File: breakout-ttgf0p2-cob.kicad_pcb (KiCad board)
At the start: 4 copper layers, 50 x 50 mm, 105 parts, among them J1 Conn_01x12, J2 DF12NB-60DS-0.5V_51, J3 DF12NB-50DS-0.5V_51, U1 AP2112K-3.3, U2 AP2112K-3.3, U3 TT_GF_0p2_ASIC, U4 24LC02

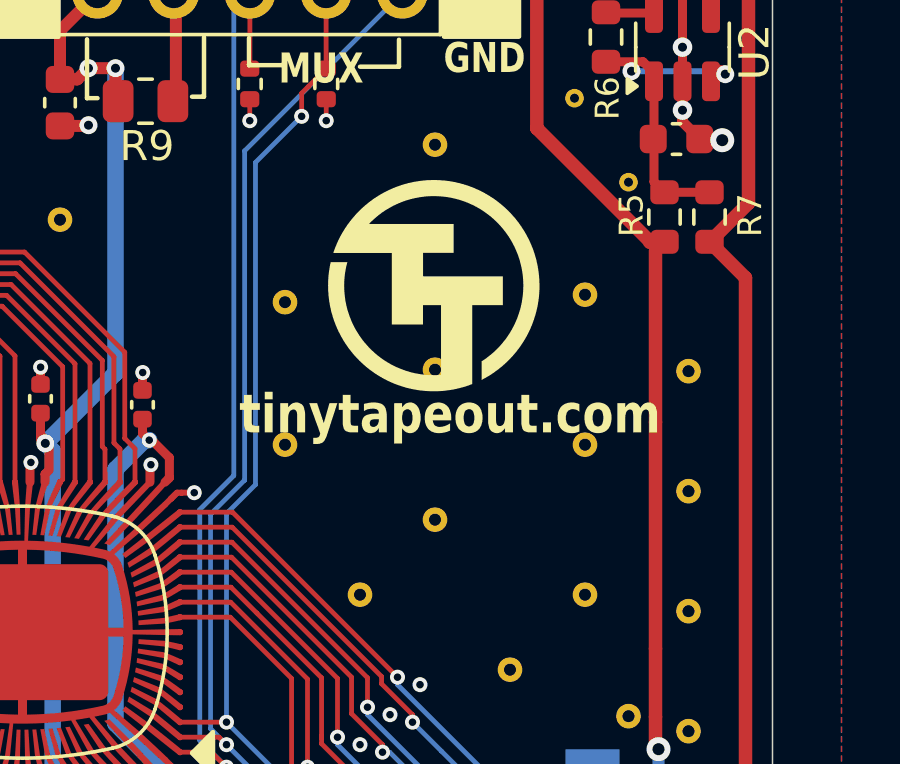
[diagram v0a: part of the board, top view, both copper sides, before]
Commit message: add tillitis logo
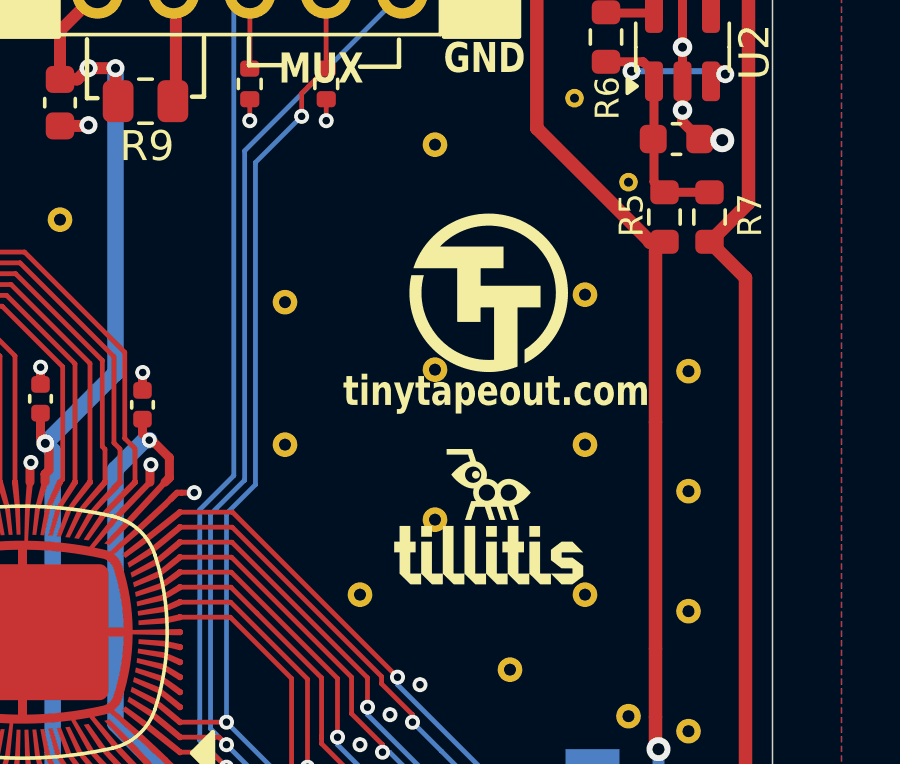
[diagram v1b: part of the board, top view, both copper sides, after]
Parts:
- added TILL1: Tillitis_logo, Logos:tillitis_logo, F.Cu at (153.5, 70.4)
- moved TTLOGO1 1.85 mm to (153.6, 62.7)

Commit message: implement fixes suggested by Sylvain
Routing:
- net +5V: track 89.4 -> 90.4 mm

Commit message: add production files
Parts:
- STITCH02, STITCH06, STITCH07, STITCH08, STITCH10, STITCH14, STITCH15, STITCH16, STITCH17, STITCH18, STITCH20, STITCH21, STITCH23, STITCH32, STITCH36, STITCH37, STITCH38, STITCH39, STITCH40, STITCH41, STITCH42, STITCH43, STITCH44, STITCH45, STITCH47, STITCH49, STITCH51, STITCH52, STITCH53, STITCH54, STITCH57: renamed from ?; value (none) -> StitchingVia-0.4mmDrill; footprint (none) -> flyingcarsfootprints:StitchingVia-0.4mmDrill
- renumbered STITCH7 to STITCH01, STITCH14 to STITCH03, STITCH17 to STITCH04, STITCH10 to STITCH05, STITCH01 to STITCH09, STITCH01 to STITCH11, STITCH11 to STITCH12, STITCH01 to STITCH13, STITCH3 to STITCH19, STITCH01 to STITCH22, STITCH12 to STITCH24, STITCH13 to STITCH25, STITCH6 to STITCH26, STITCH19 to STITCH27, STITCH01 to STITCH28, STITCH01 to STITCH29, STITCH2 to STITCH30, STITCH9 to STITCH31, STITCH01 to STITCH33, STITCH15 to STITCH34, STITCH18 to STITCH35, STITCH4 to STITCH46, STITCH5 to STITCH48, STITCH8 to STITCH50, STITCH18 to STITCH55, STITCH16 to STITCH56, STITCHSM01 to STITCHSM02, STITCHSM01 to STITCHSM03
